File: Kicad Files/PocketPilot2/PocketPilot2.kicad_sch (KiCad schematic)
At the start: 32 parts, among them P1 Conn_02x18_Odd_Even, P2 Conn_02x18_Odd_Even, Q1 BC548, U1 GY-912

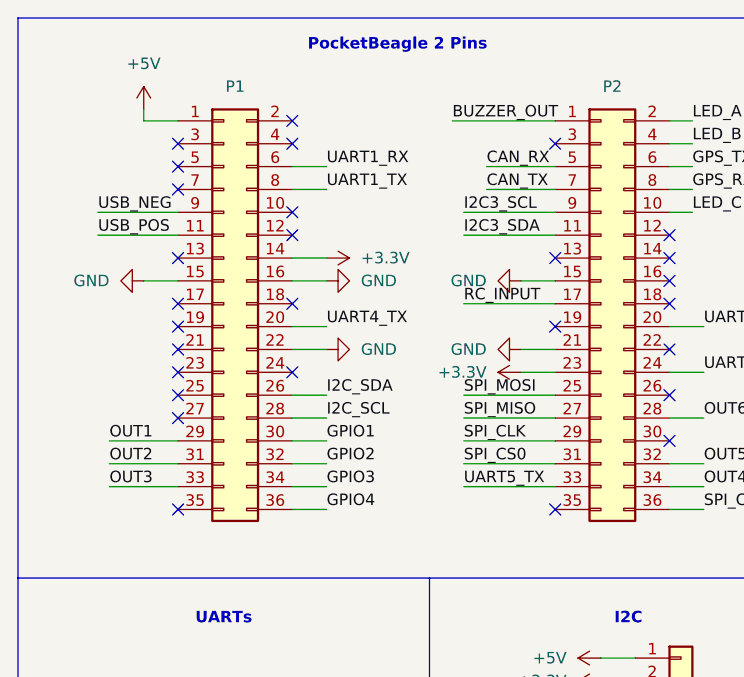
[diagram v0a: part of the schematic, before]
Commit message: Update to version to 1.1 Update GPIO pins
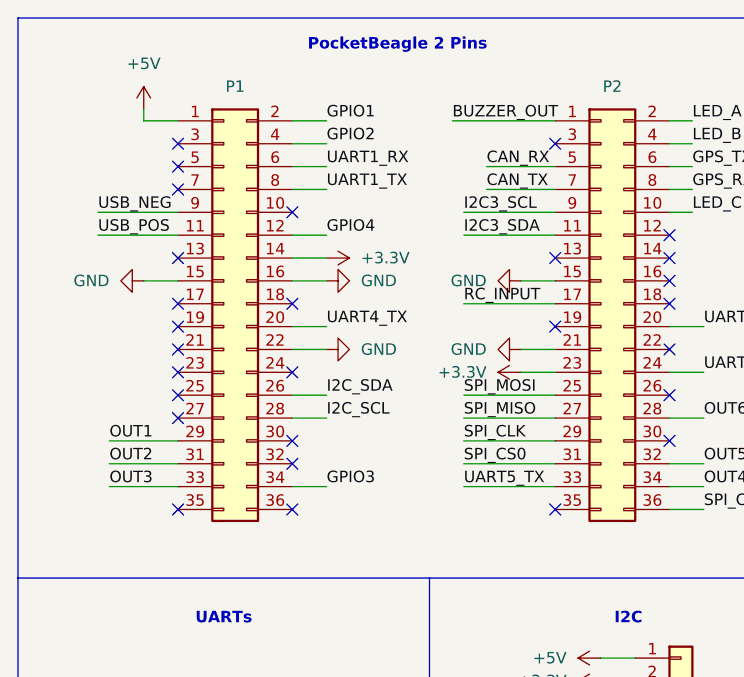
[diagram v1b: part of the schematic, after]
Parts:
- U1: footprint Connector_PinHeader_2.54mm:PinHeader_1x08_P2.54mm_Vertical -> Connector_PinSocket_2.54mm:PinSocket_1x08_P2.54mm_Vertical
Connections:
- net GPIO1: now also P1.2 (Pin_2); no longer P1.30 (Pin_30)
- net GPIO2: now also P1.4 (Pin_4); no longer P1.32 (Pin_32)
- net GPIO4: now also P1.12 (Pin_12); no longer P1.36 (Pin_36)
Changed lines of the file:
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@@
 		(title "PocketPilot2 - DIY Cape for Ardupilot")
 		(date "2025-06-30")
-		(rev "1.0")
+		(rev "1.1")
 		(comment 1 "juvinski®")
 		(comment 3 "https://github.com/juvinski/pbboard")
@@
 	)
 	(no_connect
+		(at 44.45 63.5)
+	)
+	(no_connect
 		(at 86.36 40.64)
 	)
@@
 	)
 	(no_connect
+		(at 44.45 60.96)
+	)
+	(no_connect
 		(at 31.75 68.58)
 	)
@@
 	)
 	(no_connect
-		(at 31.75 53.34)
+		(at 44.45 68.58)
 	)
 	(no_connect
-		(at 44.45 53.34)
+		(at 31.75 53.34)
 	)
 	(no_connect
-		(at 44.45 25.4)
+		(at 44.45 53.34)
 	)
 	(no_connect
@@
 	)
 	(no_connect
-		(at 44.45 38.1)
-	)
-	(no_connect
 		(at 31.75 33.02)
 	)
@@
 	)
 	(no_connect
-		(at 44.45 27.94)
-	)
-	(no_connect
 		(at 31.75 55.88)
 	)
@@
 	(wire
 		(pts
-			(xy 44.45 68.58) (xy 48.26 68.58)
+			(xy 66.04 30.48) (xy 73.66 30.48)
 		)
 		(stroke
@@
 	(wire
 		(pts
-			(xy 66.04 30.48) (xy 73.66 30.48)
+			(xy 69.85 43.18) (xy 73.66 43.18)
 		)
 		(stroke
@@
 	(wire
 		(pts
-			(xy 69.85 43.18) (xy 73.66 43.18)
+			(xy 62.23 25.4) (xy 73.66 25.4)
 		)
 		(stroke
@@
 	(wire
 		(pts
-			(xy 62.23 25.4) (xy 73.66 25.4)
+			(xy 130.81 93.98) (xy 130.81 102.87)
 		)
 		(stroke
@@
 	(wire
 		(pts
-			(xy 130.81 93.98) (xy 130.81 102.87)
+			(xy 132.08 142.24) (xy 140.97 142.24)
 		)
 		(stroke
@@
 	(wire
 		(pts
-			(xy 132.08 142.24) (xy 140.97 142.24)
+			(xy 194.31 138.43) (xy 196.85 138.43)
 		)
 		(stroke
@@
 	(wire
 		(pts
-			(xy 194.31 138.43) (xy 196.85 138.43)
+			(xy 44.45 38.1) (xy 48.26 38.1)
 		)
 		(stroke
@@
 		)
 	)
-	(wire
-		(pts
-			(xy 44.45 60.96) (xy 48.26 60.96)
-		)
-		(stroke
-			(width 0)
-			(type default)
-		)
-	)
 	(polyline
 		(pts
@@
 	(wire
 		(pts
+			(xy 44.45 27.94) (xy 48.26 27.94)
+		)
+		(stroke
+			(width 0)
+			(type default)
+		)
+	)
+	(wire
+		(pts
 			(xy 22.86 115.57) (xy 33.02 115.57)
 		)
@@
 	(wire
 		(pts
-			(xy 44.45 63.5) (xy 48.26 63.5)
+			(xy 118.11 54.61) (xy 127 54.61)
 		)
 		(stroke
@@
 	(wire
 		(pts
-			(xy 118.11 54.61) (xy 127 54.61)
+			(xy 63.5 66.04) (xy 73.66 66.04)
 		)
 		(stroke
@@
 		)
 	)
-	(wire
+	(polyline
 		(pts
-			(xy 63.5 66.04) (xy 73.66 66.04)
+			(xy 167.64 153.67) (xy 167.64 76.2)
 		)
 		(stroke
@@
 		)
 	)
-	(polyline
+	(wire
 		(pts
-			(xy 167.64 153.67) (xy 167.64 76.2)
+			(xy 44.45 25.4) (xy 48.26 25.4)
 		)
 		(stroke
@@
 	)
 	(label "GPIO4"
-		(at 48.26 68.58 0)
+		(at 48.26 38.1 0)
 		(effects
 			(font
@@
 	)
 	(label "GPIO1"
-		(at 48.26 60.96 0)
+		(at 48.26 25.4 0)
 		(effects
 			(font
@@
 	)
 	(label "GPIO2"
-		(at 48.26 63.5 0)
+		(at 48.26 27.94 0)
 		(effects
 			(font
@@
 			)
 		)
-		(property "Footprint" "Connector_PinHeader_2.54mm:PinHeader_1x08_P2.54mm_Vertical"
+		(property "Footprint" "Connector_PinSocket_2.54mm:PinSocket_1x08_P2.54mm_Vertical"
 			(at 132.08 49.53 0)
 			(effects

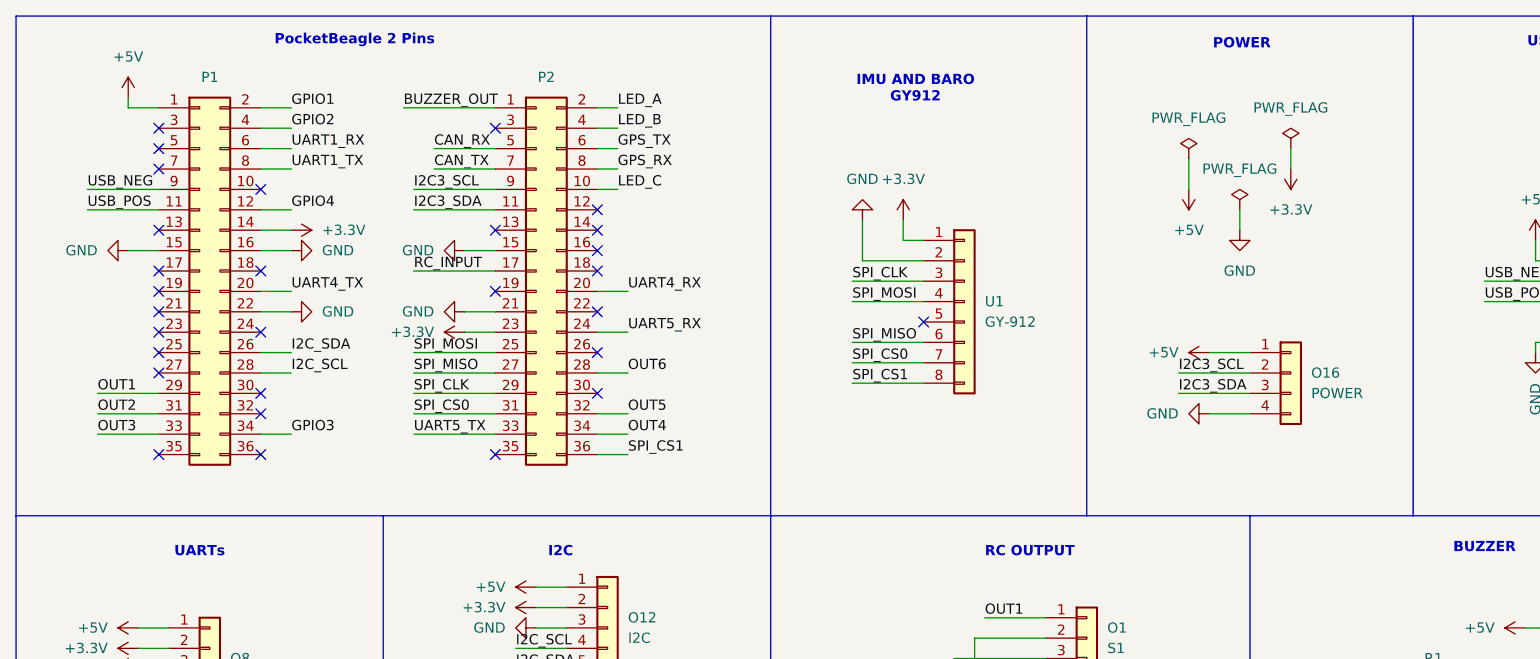
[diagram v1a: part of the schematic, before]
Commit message: Version 1.2 release 	Update board to add analog power sensing. 	Update images and instructions.
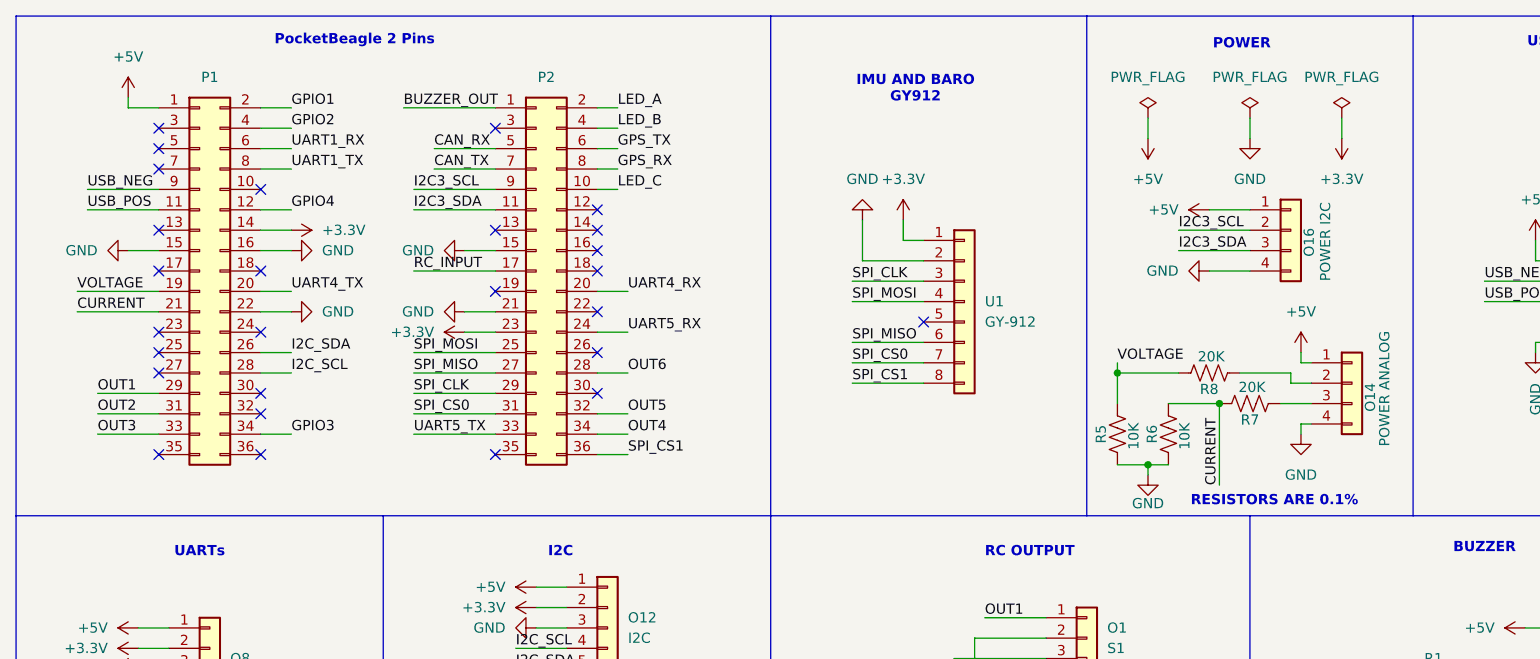
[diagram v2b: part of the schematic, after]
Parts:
- added O14: POWER ANALOG, Connector_PinHeader_2.54mm:PinHeader_1x04_P2.54mm_Vertical, symbol Connector_Generic:Conn_01x04
- added R5, R6: 10K, Resistor_THT:R_Axial_DIN0204_L3.6mm_D1.6mm_P5.08mm_Horizontal, symbol Device:R_US
- added R7, R8: 20K, Resistor_THT:R_Axial_DIN0204_L3.6mm_D1.6mm_P5.08mm_Horizontal, symbol Device:R_US
- O16: value POWER -> POWER I2C
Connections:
- net +5V: now also O14.1 (Pin_1)
- net GND: now also O14.4 (Pin_4), R5.1, R6.1
- net VOLTAGE: now reaches P1.19 (Pin_19)
- net VOLTAGE: now also R5.2, R8.2
- net CURRENT: now reaches P1.21 (Pin_21)
- net CURRENT: now also R6.2, R7.2
- new net: O14.2 (Pin_2), R8.1
- new net: O14.3 (Pin_3), R7.1
- no-connect marks 30 -> 28
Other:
- note added: "RESISTORS ARE 0.1%"
- moved on the sheet: O16
